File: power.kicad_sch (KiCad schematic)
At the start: 47 parts, among them J10 Display, J11 Rotary_Encoder, J12 Water_Pump, J13 Fan_Continous, J2 mist, J3 Led, J4 Vin, J5 Temp, J5 Temp2, J5 Water_Level, J8 Fan_Exhaust, Q1 NMOS, Q2 NMOS, Q3 NMOS, Q4 NMOS, Q5 NMOS, Q6 NMOS, U3 DS3231M

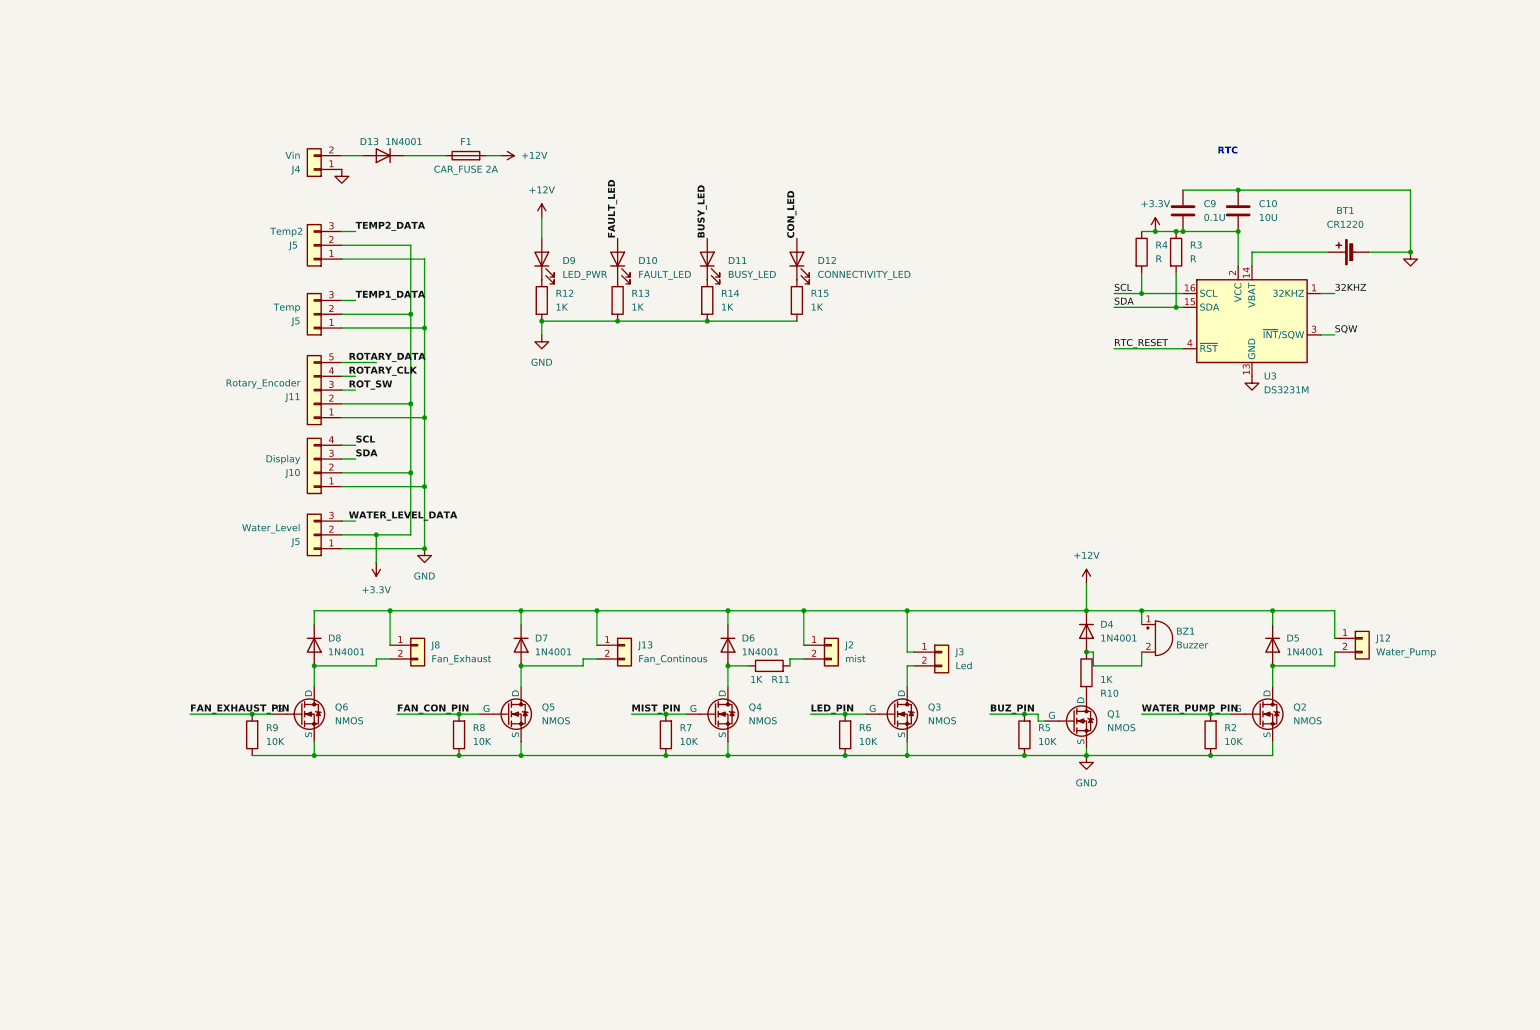
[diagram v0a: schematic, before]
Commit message: Power Section done + added backup lipo
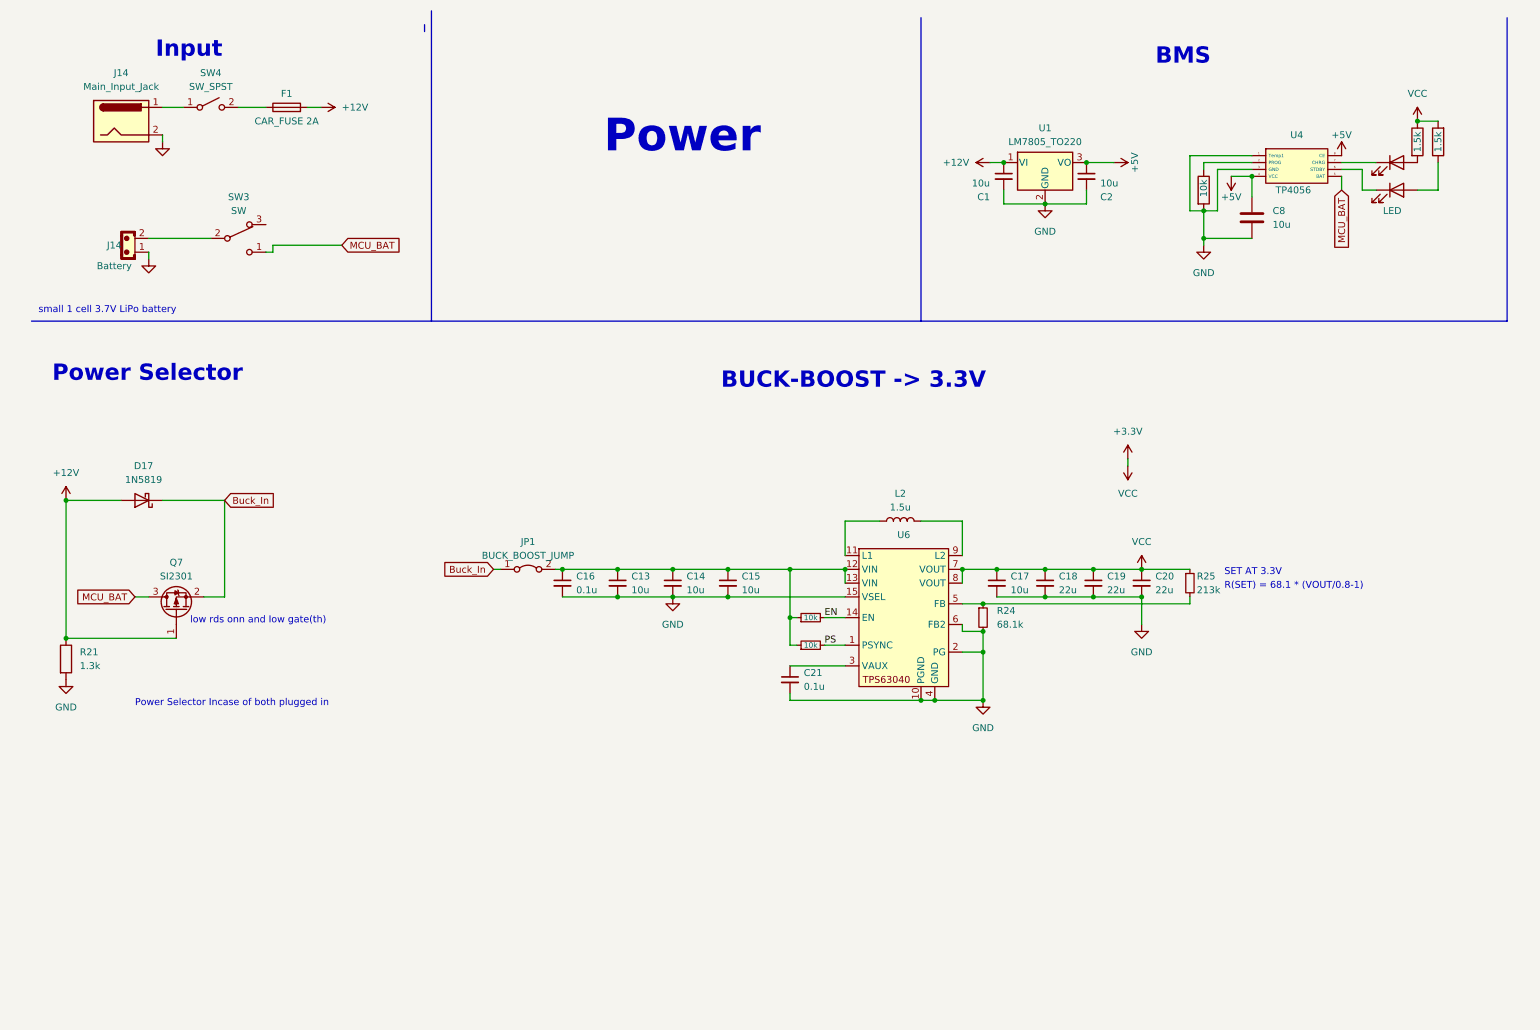
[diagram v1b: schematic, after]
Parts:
- removed BT1: CR1220, symbol Device:Battery_Cell
- removed BZ1: Buzzer, symbol Device:Buzzer
- removed C10: 10U, symbol Device:C
- removed C9: 0.1U, symbol Device:C
- removed D10: FAULT_LED, symbol Device:LED
- removed D11: BUSY_LED, symbol Device:LED
- removed D12: CONNECTIVITY_LED, symbol Device:LED
- removed D13, D4, D5, D6, D7, D8: 1N4001, Diode_THT:D_DO-41_SOD81_P10.16mm_Horizontal, symbol Diode:1N4001
- removed D9: LED_PWR, symbol Device:LED
- removed J10: Display, symbol Connector_Generic:Conn_01x04
- removed J11: Rotary_Encoder, symbol Connector_Generic:Conn_01x05
- removed J12: Water_Pump, symbol Connector_Generic:Conn_01x02
- removed J13: Fan_Continous, symbol Connector_Generic:Conn_01x02
- removed J2: mist, symbol Connector_Generic:Conn_01x02
- removed J3: Led, symbol Connector_Generic:Conn_01x02
- removed J4: Vin, symbol Connector_Generic:Conn_01x02
- removed J5: Temp2, symbol Connector_Generic:Conn_01x03
- removed J5: Temp, symbol Connector_Generic:Conn_01x03
- removed J5: Water_Level, symbol Connector_Generic:Conn_01x03
- removed J8: Fan_Exhaust, symbol Connector_Generic:Conn_01x02
- removed Q1, Q2, Q3, Q4, Q5, Q6: NMOS, symbol Simulation_SPICE:NMOS
- removed R10, R11, R12, R13, R14, R15: 1K, symbol Device:R
- removed R2, R5, R6, R7, R8, R9: 10K, symbol Device:R
- removed R3, R4: R, symbol Device:R
- removed U3: DS3231M, Package_SO:SOIC-16W_7.5x10.3mm_P1.27mm, symbol Timer_RTC:DS3231M
- added C1, C13, C14, C15, C17, C2: 10u, symbol Device:C_Small
- added C16, C21: 0.1u, symbol Device:C_Small
- added C18, C19, C20: 22u, symbol Device:C_Small
- added C8: 10u, symbol Device:C
- added D15, D16: LED, symbol Device:LED
- added D17: 1N5819, Diode_THT:D_DO-41_SOD81_P10.16mm_Horizontal, symbol Diode:1N5819
- added J14: Battery, Connector_JST:JST_EH_B2B-EH-A_1x02_P2.50mm_Vertical, symbol PCM_SL_Connectors:JST_02
- added J14: Main_Input_Jack, symbol Connector:Jack-DC
- added JP1: BUCK_BOOST_JUMP, symbol Jumper:Jumper_2_Bridged
- added L2: 1.5u, symbol Device:L
- added Q7: SI2301, Package_TO_SOT_SMD:SOT-23, symbol Transistor_FET:Si2319CDS
- added R16: 10k, symbol Device:R
- added R17, R18: 1.5k, symbol Device:R
- added R21: 1.3k, symbol Device:R
- added R22, R23: 10k, symbol Device:R_Small
- added R24: 68.1k, symbol Device:R_Small
- added R25: 213k, symbol Device:R_Small
- added SW3: SW, Button_Switch_SMD:Nidec_Copal_CAS-120A, symbol Switch:SW_Nidec_CAS-120A1
- added SW4: SW_SPST, symbol Switch:SW_SPST
- added U1: LM7805_TO220, Package_TO_SOT_THT:TO-220F-3_Horizontal_TabDown, symbol Regulator_Linear:LM7805_TO220
- added U4: TP4056, symbol Custom:TP4056
- added U6: ~, symbol Custom:TPS63070
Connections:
- net +12V: now also C1.1, D17.2 (A), Q7.1 (G), R21.1, U1.1 (VI)
- net +3.3V: now also C17.1, C18.1, C19.1, C20.1, R17.2, R18.1, R25.1, U6.7 (VOUT), U6.8 (VOUT)
- net GND: now also C1.2, C13.2, C14.2, C15.2, C16.2, C17.2, C18.2, C19.2, C2.2, C20.2, C21.2, C8.2, J14.1, J14.2, R16.2, R21.2, R24.2, U1.2 (GND), U4.1 (Temp1), U4.3 (GND), U6.10 (PGND), U6.15 (VSEL), U6.2 (PG), U6.4 (GND), U6.6 (FB2)
- net at F1.1: now also SW4.2 (B)
- new net: R16.1, U4.2 (PROG)
- new net: R24.1, R25.2, U6.5 (FB)
- new net: C21.1, U6.3 (VAUX)
- new net: J14.2, SW3.2 (B)
- new net: D15.1 (K), U4.7 (CHRG)
- new net: D15.2 (A), R18.2
- new net: D16.1 (K), U4.6 (STDBY)
- new net: L2.1, U6.11 (L1)
- new net: C13.1, C14.1, C15.1, C16.1, JP1.2 (B), R22.1, R23.1, U6.12 (VIN), U6.13 (VIN)
- new net: L2.2, U6.9 (L2)
- new net: J14.1, SW4.1 (A)
- new net: D16.2 (A), R17.1
- new net +5V: C2.1, C8.1, U1.3 (VO), U4.4 (VCC), U4.8 (CE)
- new net Buck_In: D17.1 (K), JP1.1 (A), Q7.2 (S)
- new net EN: R23.2, U6.14 (EN)
- new net MCU_BAT: Q7.3 (D), SW3.1 (C), U4.5 (BAT)
- new net PS: R22.2, U6.1 (PSYNC)
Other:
- note added: "BMS"
- note added: "BUCK-BOOST -> 3.3V"
- note added: "Input"
- note added: "Power"
- note added: "Power Selector"
- note added: "Power Selector Incase of both plugged in"
- note added: "R(SET) = 68.1 * (VOUT/0.8-1)"
- note added: "SET AT 3.3V"
- note added: "low rds onn and low gate(th)"
- note added: "small 1 cell 3.7V LiPo battery"
- note removed: "RTC"

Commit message: added io expander + rtc + fuel guage
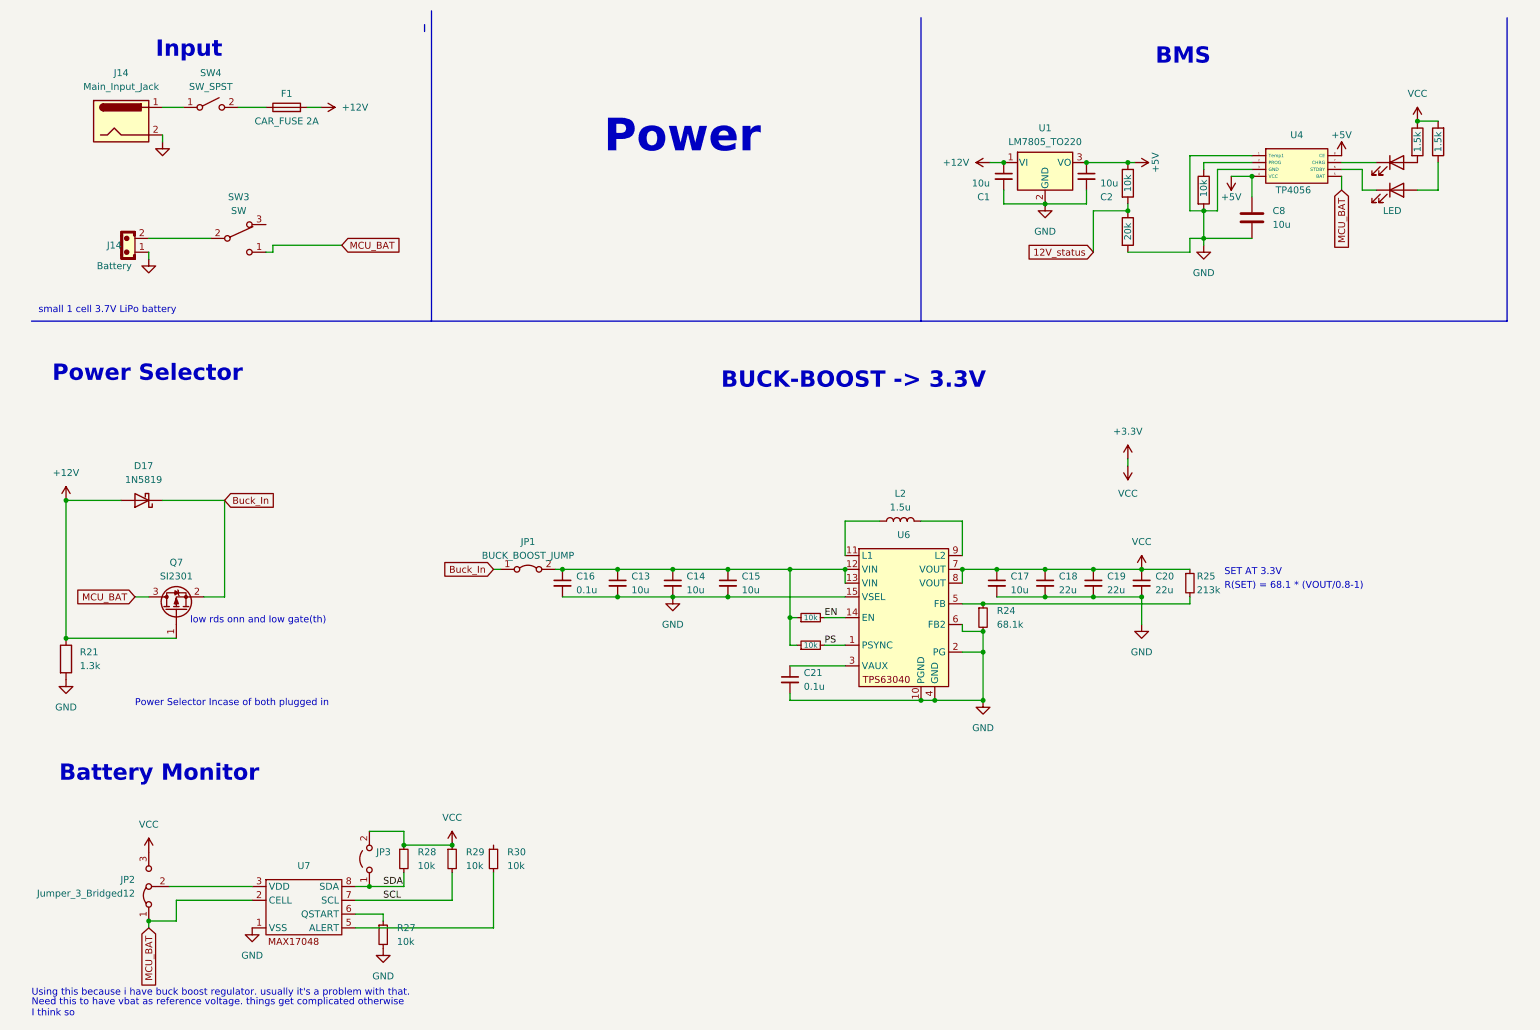
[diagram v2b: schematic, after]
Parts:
- added JP2: Jumper_3_Bridged12, symbol Jumper:Jumper_3_Bridged12
- added JP3: Jumper_2_Open, symbol Jumper:Jumper_2_Open
- added R18: 20k, symbol Device:R
- added R18: 10k, symbol Device:R
- added R27, R28, R29, R30: 10k, symbol Device:R_Small
- added U7: ~, symbol Custom:MAX17048
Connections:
- net +3.3V: now also JP2.3 (B), JP3.2 (B), R28.1, R29.1
- net +5V: now also R18.1
- net GND: now also R18.2, R27.2, U7.1 (VSS)
- net MCU_BAT: now also JP2.1 (A), U7.2 (CELL)
- new net: R30.2, U7.5 (ALERT)
- new net: JP2.2 (C), U7.3 (VDD)
- new net: R27.1, U7.6 (QSTART)
- new net 12V_status: R18.1, R18.2
- new net SCL: R29.2, U7.7 (SCL)
- new net SDA: JP3.1 (A), R28.2, U7.8 (SDA)
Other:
- note added: "Battery Monitor"
- note added: "Need this to have vbat as reference voltage. things get complicated otherwise I think so"
- note added: "Using this because i have buck boost regulator. usually it's a problem with that."

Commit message: Schematic Completed
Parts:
- removed R18: 20k, symbol Device:R
- removed R18: 1.5k, symbol Device:R
- removed R18: 10k, symbol Device:R
- added R18: 10k, symbol Device:R
- added R18: 20k, symbol Device:R
- added R18: 1.5k, symbol Device:R
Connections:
- net +3.3V is gone; now on net VCC: C17.1, C18.1, C19.1, C20.1, JP2.3 (B), JP3.2 (B), R17.2, R25.1, R28.1, R29.1, U6.7 (VOUT), U6.8 (VOUT)
- net +5V: now also R18.1
- net 12V_status: now also R18.1, R18.2
- net GND: now also R18.2
- net VCC: now reaches R30.1
- net VCC: now also R18.1
- net at D15.2 (A): now also R18.2
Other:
- note removed: "Power"
- moved on the sheet: C13, C14, C15, C16, C17, C18, C19, C20, C21, D17, JP1, JP2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
